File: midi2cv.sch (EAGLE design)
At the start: 18 parts, among them IC1 LM324N

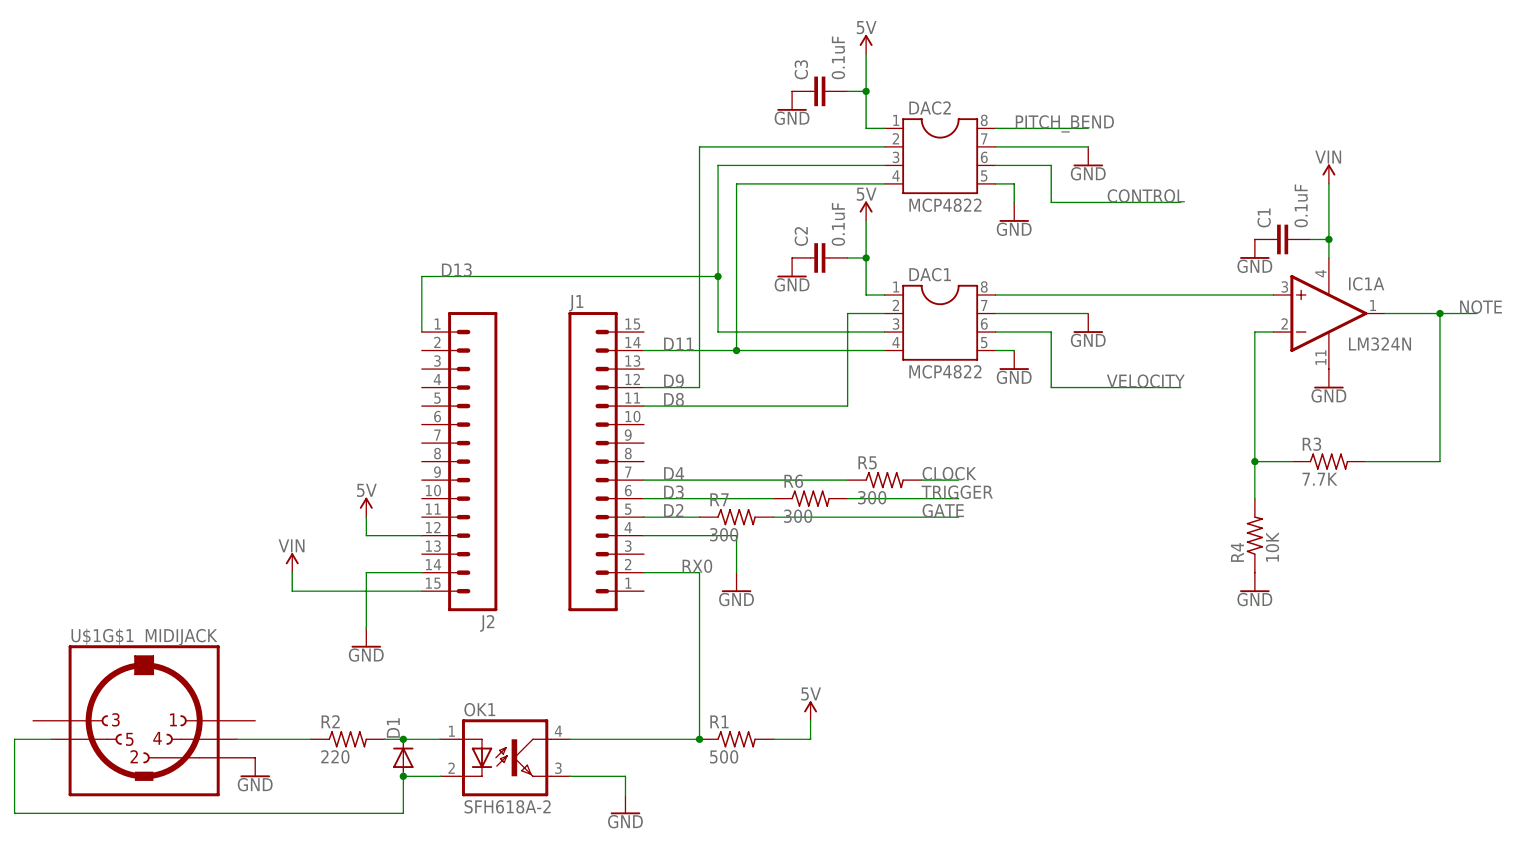
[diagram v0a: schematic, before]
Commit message: Update schematic with buffers on all DAC outputs
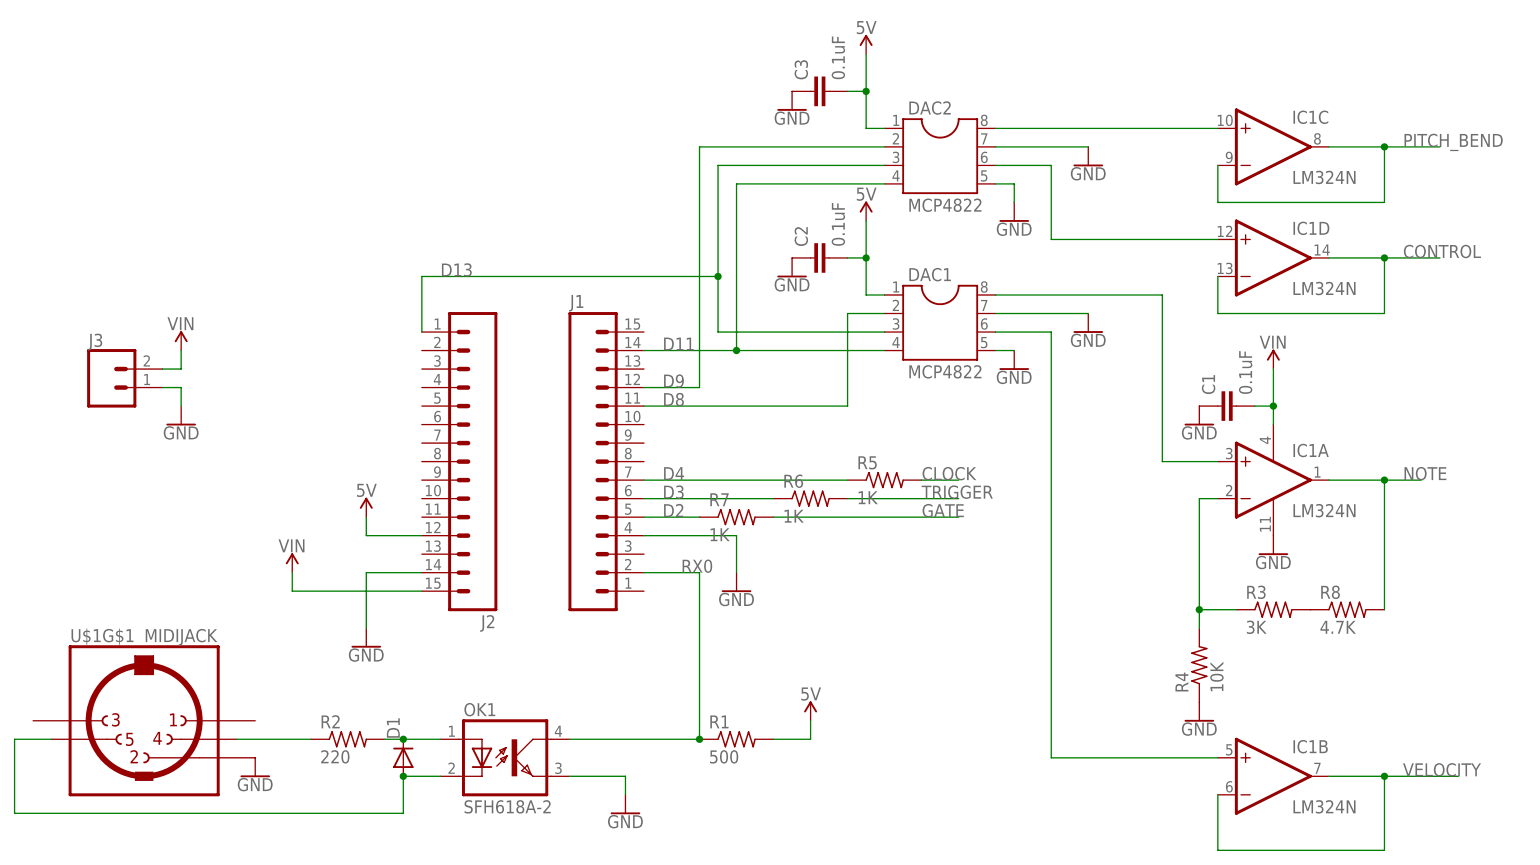
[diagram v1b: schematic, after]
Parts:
- added J3: (no value), SparkFun-Connectors:CONN_025MM
- added R8: 4.7K, resistor:R-US_0207/10
- R3: value 7.7K -> 3K
- R5, R6, R7: value 300 -> 1K
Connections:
- new net N$5: R3.2, R8.1
- new net N$7: DAC1.6, IC1B.+IN
- new net N$8: DAC2.8, IC1C.+IN
- new net N$9: DAC2.6, IC1D.+IN
- net CONTROL: now also IC1D.-IN, IC1D.OUT; no longer DAC2.6
- net GND: now also J3.1
- net NOTE: now also R8.2; no longer R3.2
- net PITCH_BEND: now also IC1C.-IN, IC1C.OUT; no longer DAC2.8
- net VELOCITY: now also IC1B.-IN, IC1B.OUT; no longer DAC1.6
- net VIN: now also J3.2
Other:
- moved on the sheet: C1, IC1A, R3, R4

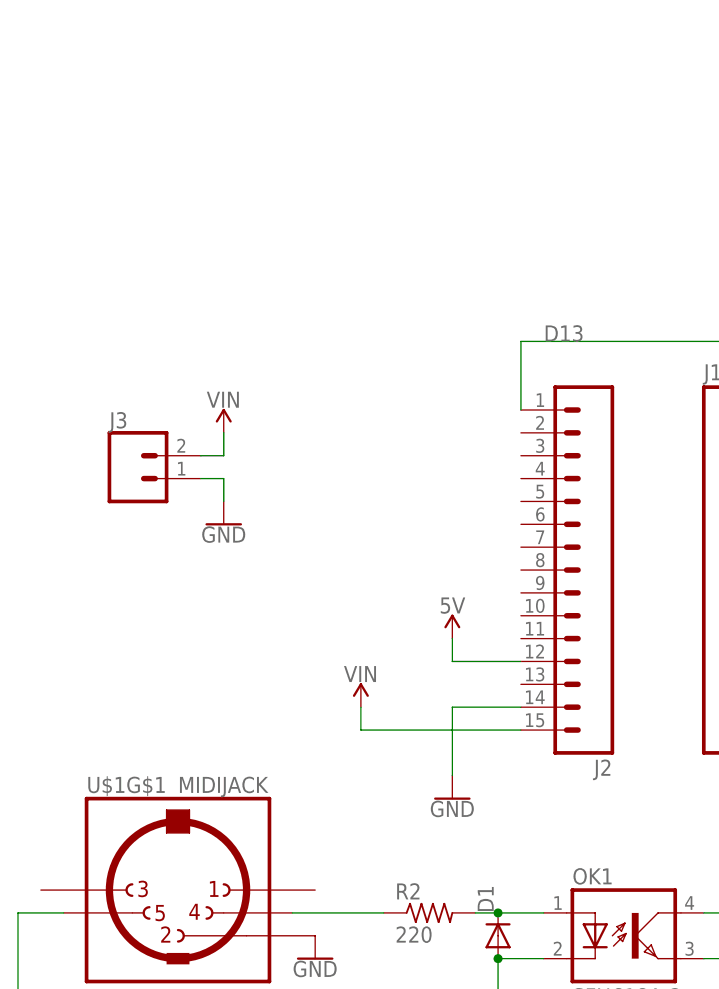
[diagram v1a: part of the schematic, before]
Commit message: Added note priority setting
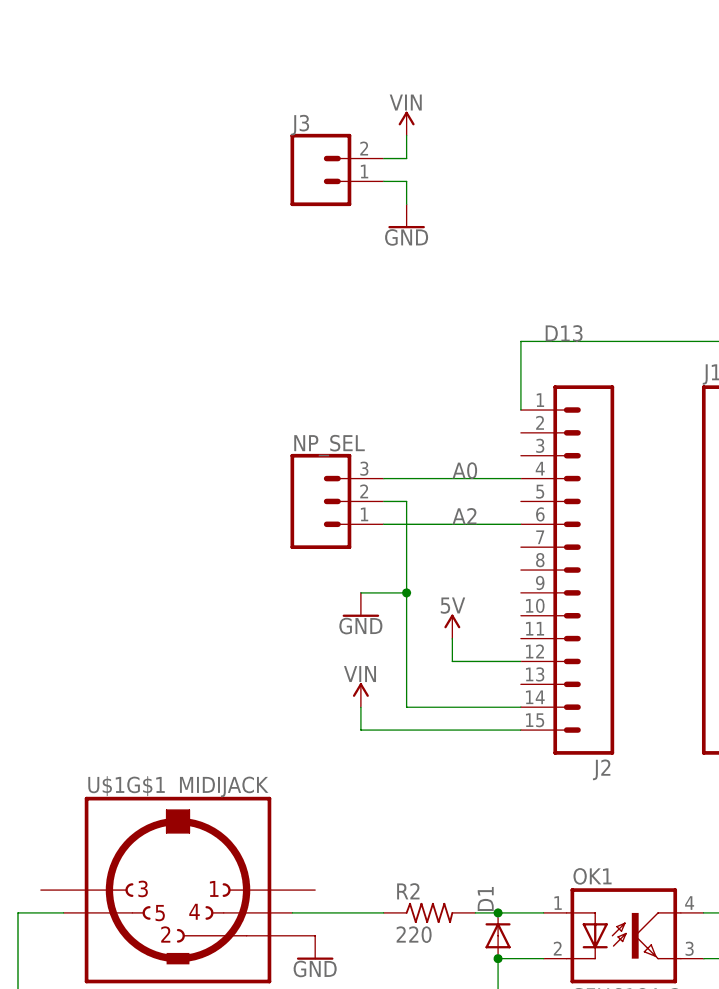
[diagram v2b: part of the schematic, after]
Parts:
- added NP_SEL: (no value), SparkFun-Connectors:CONN_03
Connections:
- new net A0: J2.4, NP_SEL.3
- new net A2: J2.6, NP_SEL.1
- net GND: now also NP_SEL.2
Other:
- moved on the sheet: J3
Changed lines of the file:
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@@
 <?xml version="1.0" encoding="utf-8"?>
 <!DOCTYPE eagle SYSTEM "eagle.dtd">
-<eagle version="8.3.2">
+<eagle version="9.0.1">
 <drawing>
 <settings>
@@
 <part name="SUPPLY7" library="SparkFun-PowerSymbols" library_urn="urn:adsk.eagle:library:530" deviceset="VIN" device=""/>
 <part name="GND13" library="SparkFun-PowerSymbols" library_urn="urn:adsk.eagle:library:530" deviceset="GND" device=""/>
+<part name="NP_SEL" library="SparkFun-Connectors" library_urn="urn:adsk.eagle:library:513" deviceset="CONN_03" device="" package3d_urn="urn:adsk.eagle:package:38063/1"/>
 </parts>
 <sheets>
@@
 <instance part="SUPPLY4" gate="G$1" x="38.1" y="50.8"/>
 <instance part="SUPPLY5" gate="G$1" x="172.72" y="78.74"/>
-<instance part="GND9" gate="1" x="48.26" y="40.64"/>
+<instance part="GND9" gate="1" x="38.1" y="60.96"/>
 <instance part="GND10" gate="1" x="99.06" y="48.26"/>
 <instance part="SUPPLY6" gate="G$1" x="48.26" y="58.42"/>
@@
 <instance part="IC1" gate="D" x="172.72" y="93.98"/>
 <instance part="R8" gate="G$1" x="182.88" y="45.72"/>
-<instance part="J3" gate="G$1" x="12.7" y="76.2"/>
-<instance part="SUPPLY7" gate="G$1" x="22.86" y="81.28"/>
-<instance part="GND13" gate="1" x="22.86" y="71.12"/>
+<instance part="J3" gate="G$1" x="33.02" y="109.22"/>
+<instance part="SUPPLY7" gate="G$1" x="43.18" y="114.3"/>
+<instance part="GND13" gate="1" x="43.18" y="104.14"/>
+<instance part="NP_SEL" gate="J$1" x="33.02" y="73.66"/>
 </instances>
 <busses>
@@
 </segment>
 <segment>
-<pinref part="GND9" gate="1" pin="GND"/>
-<wire x1="48.26" y1="43.18" x2="48.26" y2="50.8" width="0.1524" layer="91"/>
-<pinref part="J2" gate="G$1" pin="14"/>
-<wire x1="48.26" y1="50.8" x2="55.88" y2="50.8" width="0.1524" layer="91"/>
-</segment>
-<segment>
 <pinref part="J1" gate="G$1" pin="4"/>
 <pinref part="GND10" gate="1" pin="GND"/>
@@
 <pinref part="J3" gate="G$1" pin="1"/>
 <pinref part="GND13" gate="1" pin="GND"/>
-<wire x1="20.32" y1="76.2" x2="22.86" y2="76.2" width="0.1524" layer="91"/>
-<wire x1="22.86" y1="76.2" x2="22.86" y2="73.66" width="0.1524" layer="91"/>
+<wire x1="40.64" y1="109.22" x2="43.18" y2="109.22" width="0.1524" layer="91"/>
+<wire x1="43.18" y1="109.22" x2="43.18" y2="106.68" width="0.1524" layer="91"/>
+</segment>
+<segment>
+<pinref part="J2" gate="G$1" pin="14"/>
+<wire x1="43.18" y1="50.8" x2="55.88" y2="50.8" width="0.1524" layer="91"/>
+<pinref part="NP_SEL" gate="J$1" pin="2"/>
+<wire x1="40.64" y1="73.66" x2="43.18" y2="73.66" width="0.1524" layer="91"/>
+<wire x1="43.18" y1="50.8" x2="43.18" y2="63.5" width="0.1524" layer="91"/>
+<pinref part="GND9" gate="1" pin="GND"/>
+<wire x1="43.18" y1="63.5" x2="43.18" y2="73.66" width="0.1524" layer="91"/>
+<wire x1="38.1" y1="63.5" x2="43.18" y2="63.5" width="0.1524" layer="91"/>
+<junction x="43.18" y="63.5"/>
 </segment>
 </net>
@@
 <pinref part="J3" gate="G$1" pin="2"/>
 <pinref part="SUPPLY7" gate="G$1" pin="VIN"/>
-<wire x1="20.32" y1="78.74" x2="22.86" y2="78.74" width="0.1524" layer="91"/>
-<wire x1="22.86" y1="78.74" x2="22.86" y2="81.28" width="0.1524" layer="91"/>
+<wire x1="40.64" y1="111.76" x2="43.18" y2="111.76" width="0.1524" layer="91"/>
+<wire x1="43.18" y1="111.76" x2="43.18" y2="114.3" width="0.1524" layer="91"/>
 </segment>
 </net>
@@
 </segment>
 </net>
+<net name="A0" class="0">
+<segment>
+<pinref part="NP_SEL" gate="J$1" pin="3"/>
+<pinref part="J2" gate="G$1" pin="4"/>
+<wire x1="40.64" y1="76.2" x2="55.88" y2="76.2" width="0.1524" layer="91"/>
+<label x="48.26" y="76.2" size="1.778" layer="95"/>
+</segment>
+</net>
+<net name="A2" class="0">
+<segment>
+<pinref part="NP_SEL" gate="J$1" pin="1"/>
+<pinref part="J2" gate="G$1" pin="6"/>
+<wire x1="40.64" y1="71.12" x2="55.88" y2="71.12" width="0.1524" layer="91"/>
+<label x="48.26" y="71.12" size="1.778" layer="95"/>
+</segment>
+</net>
